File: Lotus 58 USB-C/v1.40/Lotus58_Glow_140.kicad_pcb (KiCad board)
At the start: 2 copper layers, 139.1 x 107.7 mm, 119 parts, among them J3 USB_C_Receptacle_USB2.0, P1 OLED, SW1 Kailh hotswap MX socket, SW10 Kailh hotswap MX socket, SW11 Kailh hotswap MX socket, SW12 Kailh hotswap MX socket, SW13 Kailh hotswap MX socket, SW14 Kailh hotswap MX socket, SW15 Kailh hotswap MX socket, SW16 Kailh hotswap MX socket, SW17 Kailh hotswap MX socket, SW18 Kailh hotswap MX socket, SW19 Kailh hotswap MX socket, SW2 Kailh hotswap MX socket, SW20 Kailh hotswap MX socket, SW21 Kailh hotswap MX socket, SW22 Kailh hotswap MX socket, SW23 Kailh hotswap MX socket, SW24 Kailh hotswap MX socket, SW25 Kailh hotswap MX socket, SW26 Kailh hotswap MX socket, SW27 Kailh hotswap MX socket, SW28 Kailh hotswap MX socket, SW29 Kailh hotswap MX socket, SW3 Kailh hotswap MX socket, SW30 Rotary_Encoder_Switch, SW31 Rotary_Encoder_Switch, SW32 MSK12C02, SW33 MSK12C02, SW4 Kailh hotswap MX socket, SW5 Kailh hotswap MX socket, SW6 Kailh hotswap MX socket, SW7 Kailh hotswap MX socket, SW8 Kailh hotswap MX socket, SW9 Kailh hotswap MX socket, U1 ProMicro, U2 SRV05-4

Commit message: L58 C v1.40
fix silkscreen
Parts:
- FB1: value Ferrite Bead -> Ferrite Beads
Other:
- board text added: "LEFT HAND Solder jumpers on this side FIRST! Place controller facing PCB. Encoder is placed on TOP of PCB! Close for OLED on LEFT HAND"
- board text added: "RIGHT HAND Solder jumpers on this side FIRST! Place controller facing PCB. Encoder is placed on TOP of PCB! Close for OLED on RIGHT HAND"
- board text removed: "Close for OLED on LEFT HAND"
- board text removed: "Close for OLED on RIGHT HAND"
- board text removed: "Encoder is placed on TOP of PCB!"
- board text removed: "RIGHT HAND Solder jumpers FIRST! THEN Place controller facing PCB."
- board text removed: "locked"
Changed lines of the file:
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@@
         (effects (font (size 1 1) (thickness 0.15)))
     )
-    (fp_text user "${REFERENCE}" (at -4.17 5.76 90) (layer "F.SilkS")
+    (fp_text user "${REFERENCE}" (at -4.17 5.76 90) (layer "F.SilkS") hide
         (effects (font (size 1 1) (thickness 0.15)))
     )
@@
         (effects (font (size 1 1) (thickness 0.15)))
     )
-    (fp_text value "Ferrite Bead" (at 2.51 -0.77) (layer "F.SilkS")
-        (effects (font (size 1 1) (thickness 0.15)))
+    (fp_text value "Ferrite Beads " (at 0.48 -3.31) (layer "F.SilkS")
+        (effects (font (size 0.75 0.75) (thickness 0.12)))
     )
     (fp_text user "${REFERENCE}" (at 0 0 -360) (layer "F.Fab")
@@
     (effects (font (size 1.2 1.2) (thickness 0.25)) (justify mirror))
   )
-  (gr_text "Close for \nOLED on RIGHT HAND" (at 91.575 70.475) (layer "B.SilkS")
-    (effects (font (size 0.75 0.75) (thickness 0.12)) (justify mirror))
-  )
-  (gr_text "Encoder is\nplaced on\nTOP of PCB!\n" (at 91.567 57.35) (layer "B.SilkS")
-    (effects (font (size 0.75 0.75) (thickness 0.12)) (justify mirror))
-  )
   (gr_text "RIGHT HAND\nCOMPONENT SIDE" (at 88.85 114.48) (layer "B.SilkS")
     (effects (font (size 0.75 0.75) (thickness 0.12)) (justify mirror))
@@
     (effects (font (size 0.75 0.75) (thickness 0.12)) (justify left mirror))
   )
-  (gr_text "RIGHT HAND\nSolder jumpers\nFIRST!\nTHEN Place\ncontroller\nfacing PCB." (at 91.56 41.67) (layer "B.SilkS")
+  (gr_text "RIGHT HAND\nSolder jumpers\non this side\nFIRST!\n\n\n\nPlace\ncontroller\nfacing PCB.\n\n\n\nEncoder is\nplaced on\nTOP of PCB!\n\n\n\n\n\n\nClose for\nOLED \non RIGHT HAND" (at 91.567 55.65) (layer "B.SilkS")
     (effects (font (size 0.75 0.75) (thickness 0.12)) (justify mirror))
   )
@@
     (effects (font (size 0.75 0.75) (thickness 0.12)) (justify mirror))
   )
-  (gr_text "Close for\nOLED on LEFT HAND" (at 91.575 70.475) (layer "F.SilkS")
-    (effects (font (size 0.75 0.75) (thickness 0.12)))
-  )
   (gr_text "Lotus 58 Glow" (at 88.85 109.0422) (layer "F.SilkS")
     (effects (font (size 1.2 1.2) (thickness 0.25)))
   )
-  (gr_text "Encoder is\nplaced on\nTOP of PCB!" (at 91.567 57.35) (layer "F.SilkS")
-    (effects (font (size 0.75 0.75) (thickness 0.12)))
-  )
   (gr_text "3b. Solder the diodes to the COMPONENT SIDE of each hand. (Align stripe with square pad/arrow).\n3c. Solder RGB LED's as marked. Per-key RGB face UP & Glow RGB face DOWN!" (at 143.5 106.245 90) (layer "F.SilkS")
     (effects (font (size 0.75 0.75) (thickness 0.12)) (justify left))
@@
     (effects (font (size 0.75 0.75) (thickness 0.12)) (justify left))
   )
-  (gr_text locked "LEFT HAND\nSolder jumpers\nFIRST!\nTHEN Place\ncontroller\nfacing PCB." (at 91.567 41.67) (layer "F.SilkS")
+  (gr_text "LEFT HAND\nSolder jumpers\non this side\nFIRST!\n\n\n\nPlace\ncontroller\nfacing PCB.\n\n\n\nEncoder is\nplaced on\nTOP of PCB!\n\n\n\n\n\n\nClose for\nOLED \non LEFT HAND" (at 91.567 55.65) (layer "F.SilkS")
     (effects (font (size 0.75 0.75) (thickness 0.12)))
   )

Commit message: Created STEP files for 3D model
Signed-off-by: TweetyDaBird <markus.knutsson@tweety.se>
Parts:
- J3: footprint LCSC_Library:Molex-216990_GCT-USB45xx_HRO-TYPE-C-31-M-13x-PiMicro -> Keyboard Common:Molex-216990_GCT-USB45xx_HRO-TYPE-C-31-M-13x-PiMicro
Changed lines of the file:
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@@
     (pad "D" thru_hole circle (at 18.5 -3.81 270) (size 1.6 1.6) (drill 0.8) (layers "*.Cu" "*.Mask")
       (net 117 "unconnected-(P1-0-PadD)") (pinfunction "0") (pintype "no_connect"))
-    (model "${KICAD6_3RD_PARTY}/3dmodels/OLED/OLED_0.91_128x32.stp"
-      (offset (xyz 1 0 3))
-      (scale (xyz 1 1 1))
-      (rotate (xyz 0 0 180))
-    )
     (model "D:/Users/markus/Documents/KiCad/6.0/3dmodels/OLED/OLED_0.91_128x32.stp"
       (offset (xyz 1 0 2.5))
@@
     (pad "3" smd roundrect (at 2.54 -0.35) (size 0.95 1.1) (layers "F.Cu" "F.Paste" "F.Mask") (roundrect_rratio 0.05)
       (net 34 "GND") (pinfunction "3") (pintype "passive") (zone_connect 2))
-    (model "${KICAD6_3RD_PARTY}/3dmodels/YTS-A002/SWITCH_xiaobeibei.STEP"
+    (model "D:/Users/markus/Documents/KiCad/6.0/3dmodels/YTS-A002/SWITCH_xiaobeibei.STEP"
       (offset (xyz -0.27 0 -3))
       (scale (xyz 1.15 0.9 1))
@@
     (pad "NO" smd rect (at 2.2 -2.2 180) (size 0.8 1.6) (layers "F.Cu" "F.Paste" "F.Mask")
       (net 77 "/PWR_KEY") (pinfunction "NO") (pintype "power_in"))
-    (model "${KICAD6_3RD_PARTY}/3dmodels/MSK12C02/User Library-Slide-SW_SPDT.STEP"
+    (model "D:/Users/markus/Documents/KiCad/7.0/3dmodels/MSK12C02/User Library-Slide-SW_SPDT.STEP"
       (offset (xyz 0 0 0))
       (scale (xyz 1 1 1))
@@
     )
   )
-  (footprint "LCSC_Library:Molex-216990_GCT-USB45xx_HRO-TYPE-C-31-M-13x-PiMicro" (layer "F.Cu")
+  (footprint "Keyboard Common:Molex-216990_GCT-USB45xx_HRO-TYPE-C-31-M-13x-PiMicro" (layer "F.Cu")
     (at 81.167 83.75 -90)
     (property "LCSC" "C963373")
@@
     (property "ki_keywords" "usb universal serial bus type-C USB2.0")
     (attr smd)
-    (fp_text reference "J3" (at -6.858 -3.215 unlocked) (layer "F.SilkS") hide
+    (fp_text reference "J3" (at -6.858 -3.215 unlocked) (layer "F.SilkS")
         (effects (font (size 1 1) (thickness 0.15)))
     )
@@
     (pad "S1" thru_hole oval (at 5.62 -1.183 270) (size 1 2.2) (drill oval 0.6 1.8) (layers "*.Cu" "*.Mask")
       (net 94 "Net-(J3-SHIELD)") (pinfunction "SHIELD") (pintype "passive"))
-    (model "${KICAD6_3RD_PARTY}/3dmodels/HRO_TYPE-C/HRO TYPE-C-31-M-14.step"
+    (model "D:/Users/markus/Documents/KiCad/6.0/3dmodels/HRO_TYPE-C/HRO TYPE-C-31-M-14.step"
       (offset (xyz 0 -1.25 0))
       (scale (xyz 1 1 1))
@@
     (pad "3" smd roundrect (at 2.54 0.35 180) (size 0.95 1.1) (layers "B.Cu" "B.Paste" "B.Mask") (roundrect_rratio 0.05)
       (net 34 "GND") (pinfunction "3") (pintype "passive") (zone_connect 2))
-    (model "${KICAD6_3RD_PARTY}/3dmodels/YTS-A002/SWITCH_xiaobeibei.STEP"
+    (model "D:/Users/markus/Documents/KiCad/6.0/3dmodels/YTS-A002/SWITCH_xiaobeibei.STEP"
       (offset (xyz -0.27 0 -3))
       (scale (xyz 1.15 0.9 1))
@@
     (pad "NO" smd rect (at 2.2 2.2) (size 0.8 1.6) (layers "B.Cu" "B.Paste" "B.Mask")
       (net 77 "/PWR_KEY") (pinfunction "NO") (pintype "power_in"))
-    (model "${KICAD6_3RD_PARTY}/3dmodels/MSK12C02/User Library-Slide-SW_SPDT.STEP"
+    (model "D:/Users/markus/Documents/KiCad/7.0/3dmodels/MSK12C02/User Library-Slide-SW_SPDT.STEP"
       (offset (xyz 0 0 0))
       (scale (xyz 1 1 1))

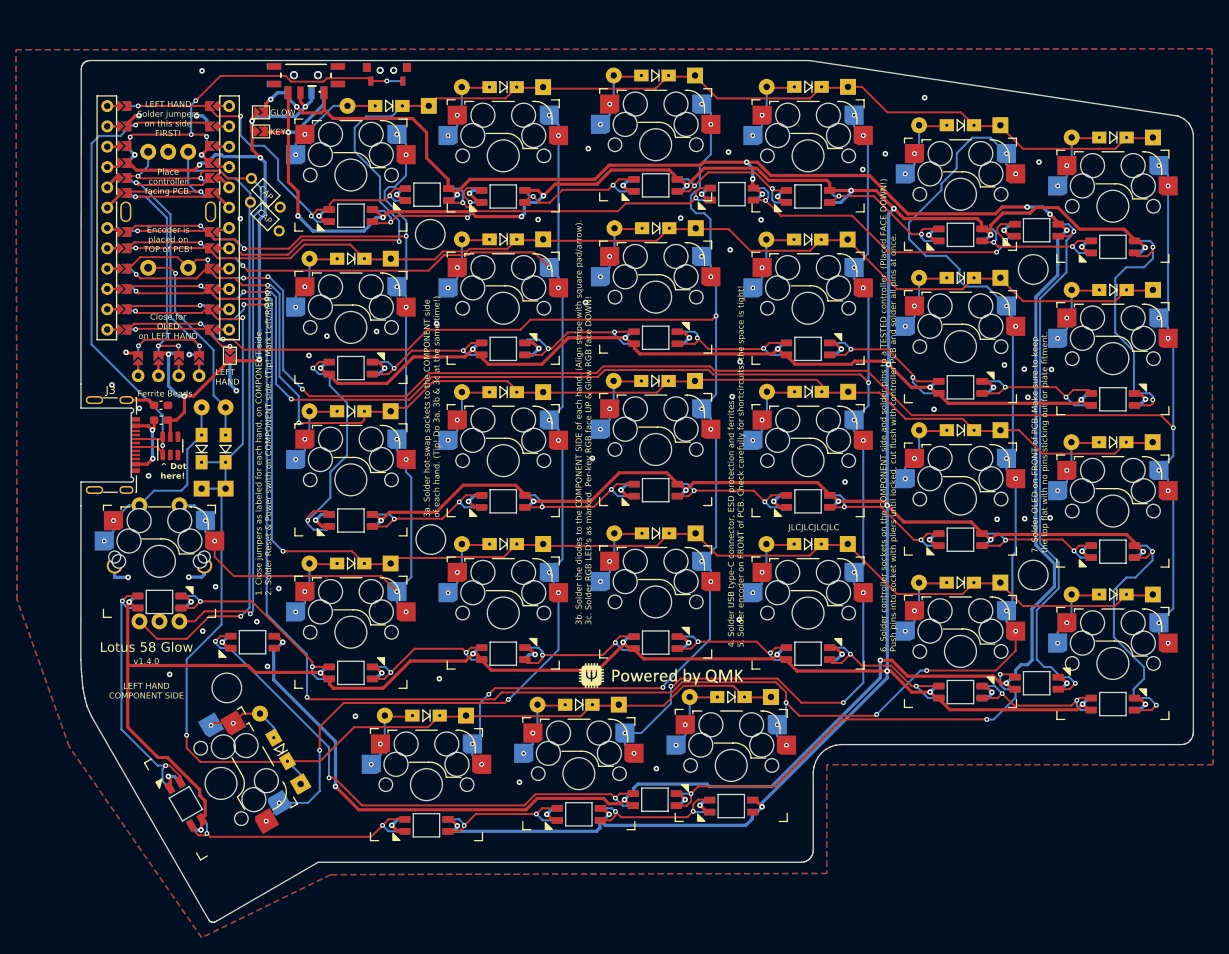
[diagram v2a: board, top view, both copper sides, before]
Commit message: Initial changes for kailh choc V1 hostswaps
* Changed footprint for switches to kailh choc V1 hotswaps
* Change per-key and underglow LED positions
* Rerouted all tracks for LEDS and switches
* Removed encoder near thumb cluster
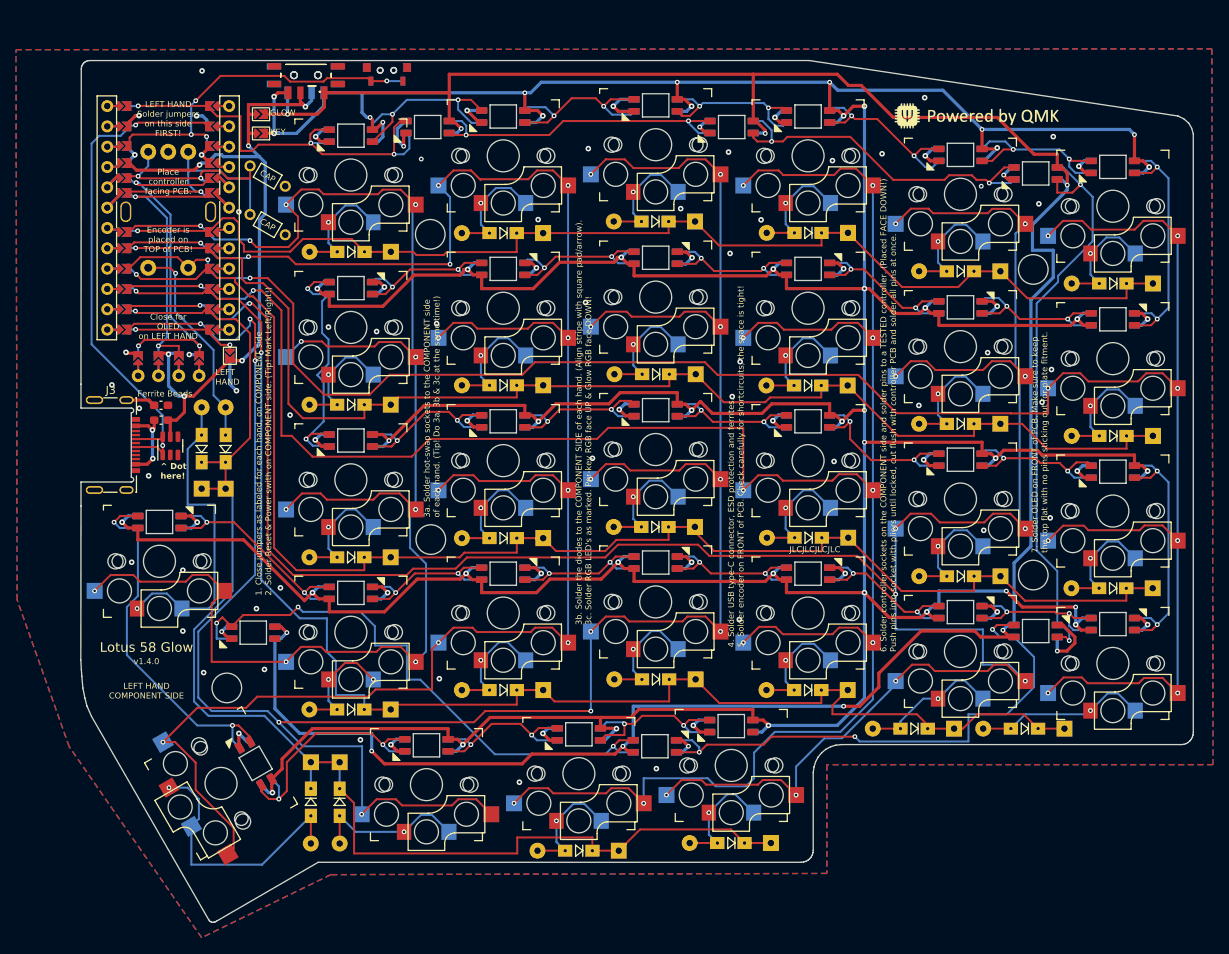
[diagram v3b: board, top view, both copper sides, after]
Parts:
- removed SW31: Rotary_Encoder_Switch, Keyboard Encoders:Encoder_Alps_EC11E_Offset_pad
- SW1: value Kailh hotswap MX socket -> Kailh hotswap Choc V1 socket; footprint Keyboard Switches:SW_MX_HotSwap_Reversible -> Spencer-Custom:SW_Kailh_Choc_V1_HotSwap_Reversible; moved to B.Cu
- SW10, SW11, SW12, SW13, SW14, SW15, SW16, SW17, SW18, SW19, SW2, SW20, SW21, SW22, SW23, SW24, SW25, SW26, SW27, SW28, SW29, SW3, SW4, SW5, SW6, SW7, SW8, SW9: value Kailh hotswap MX socket -> Kailh hotswap Choc V1 socket; footprint Keyboard Switches:SW_MX_HotSwap_Reversible -> Spencer-Custom:SW_Kailh_Choc_V1_HotSwap_Reversible
- moved Logo1 80.3 mm to (192.6, 42.6)
- moved Logo2 80.3 mm to (192.8, 42.6)
- moved D24 20.1 mm to (198.6, 119.2)
- moved D23 19.1 mm to (184.8, 119.2)
- moved D1 18.8 mm to (114.4, 59.6)
- moved D28 18.3 mm to (142.9, 134.5)
- moved D8 18.3 mm to (133.4, 76.3)
- moved D9 18.3 mm to (152.5, 74.9)
- moved D10 18.2 mm to (171.5, 76.3)
- moved D12 18.2 mm to (209.7, 82.6)
- moved D13 18.2 mm to (114.4, 97.8)
- moved D14 18.2 mm to (133.4, 95.4)
- moved D15 18.2 mm to (152.4, 94.0)
- moved D16 18.2 mm to (171.6, 95.3)
- moved D17 18.2 mm to (190.6, 100.2)
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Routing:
- net col3: track 190.0 -> 298.3 mm, vias 15 -> 14
- net col2: track 222.1 -> 299.8 mm, vias 17 -> 12
- net col4: track 175.9 -> 244.2 mm, vias 14 -> 12
- net EncA: track 93.1 -> 28.7 mm, vias 2 -> 1
- net col1: track 255.6 -> 319.3 mm, vias 17 -> 13
- net EncB: track 86.1 -> 22.5 mm, vias 3 -> 2
- net col5: track 136.4 -> 197.5 mm, vias 13 -> 11
- net col0: track 214.4 -> 266.8 mm, vias 13 -> 10
- net /PWR_KEY: track 701.1 -> 752.0 mm, vias 36 -> 44
- net GND: track 139.7 -> 165.6 mm
- net row2: track 154.1 -> 179.1 mm, vias 3 -> 1
- net Net-(D26-A): track 10.4 -> 33.8 mm, vias 2 -> 1
- net row1: track 138.1 -> 160.4 mm
- net Alt: track 24.5 -> 40.1 mm, vias 2 -> 1
- net row0: track 161.1 -> 147.2 mm, vias 2 -> 1
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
